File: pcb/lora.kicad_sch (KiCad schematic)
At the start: 57 parts, among them J1 Conn_01x04, J11 Conn_Coaxial, J2 5V, J3 Temp, J5 Temp, J6 VDD, J7 UART, J9 I2C, Q2 AO3401A, Q3 AO3401A, Q5 AO3401A, SW1 RESET, SW2 PJ, U1 ME2108C50M5G, U2 ESP32-WROOM-32D, U3 2460, U4 RFM95W-868S2

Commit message: schematic finalized
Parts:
- removed Q?: AO3400A, Package_TO_SOT_SMD:SOT-23, symbol Transistor_FET:AO3400A
- removed R?: 100, Resistor_SMD:R_0603_1608Metric, symbol Device:R_Small
- removed R?: 10k, Capacitor_SMD:C_0603_1608Metric, symbol Device:R_Small
- added C10: 2u2, Capacitor_SMD:C_0805_2012Metric, symbol Device:C_Small
- added C14, C16, C20: 100n, Capacitor_SMD:C_0603_1608Metric, symbol Device:C_Small
- added C15, C18, C8: 10u, Capacitor_SMD:C_0805_2012Metric, symbol Device:C_Small
- added C17: 100p, Capacitor_SMD:C_0603_1608Metric, symbol Device:C_Small
- added C19: 1u, Capacitor_SMD:C_0603_1608Metric, symbol Device:C_Small
- added C21, C4: 47u, Capacitor_SMD:C_1206_3216Metric, symbol Device:C_Small
- added D10, D4, D6, D7, D8, D9: D_TVS, Diode_SMD:D_0402_1005Metric, symbol Device:D_TVS
- added D3: D_MM1Z15, Diode_SMD:D_SOD-123, symbol Device:D_Zener
- added FB1: Ferrite, Inductor_SMD:L_0805_2012Metric, symbol Device:FerriteBead_Small
- added L3: 15u, OWN_PARTS:SLO0630H, symbol Device:L_Small
- added Q1: AO3401A, Package_TO_SOT_SMD:SOT-23, symbol Transistor_FET:AO3401A
- added R14, R18: 100k, Resistor_SMD:R_0603_1608Metric, symbol Device:R_Small
- added R21: 62k, Resistor_SMD:R_0603_1608Metric, symbol Device:R_Small
- added R22: 20k, Resistor_SMD:R_0603_1608Metric, symbol Device:R_Small
- added R23, R24: 1k, Capacitor_SMD:C_0603_1608Metric, symbol Device:R_Small
- added SW3: K3-1296S-E1, OWN_Parts_:K3-1296S-E1, symbol OWN_Parts_:K3-1296S-E1
- added U5: SCT2400, Package_TO_SOT_SMD:TSOT-23-6, symbol lv2842x:LV2842X
- J1: footprint (none) -> TerminalBlock_TE-Connectivity:TerminalBlock_TE_282834-4_1x04_P2.54mm_Horizontal
- J3: footprint Connector_PinHeader_2.54mm:PinHeader_1x03_P2.54mm_Horizontal -> TerminalBlock_TE-Connectivity:TerminalBlock_TE_282834-3_1x03_P2.54mm_Horizontal
- J6: footprint Connector_PinHeader_2.54mm:PinHeader_1x02_P2.54mm_Vertical -> TerminalBlock_TE-Connectivity:TerminalBlock_TE_282834-2_1x02_P2.54mm_Horizontal
- J7, J9: footprint Connector_PinHeader_2.54mm:PinHeader_1x04_P2.54mm_Vertical -> TerminalBlock_TE-Connectivity:TerminalBlock_TE_282834-4_1x04_P2.54mm_Horizontal
- U3: footprint SamacSys_Parts:2460 -> 2460
- gave numbers to parts that had none: 1
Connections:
- net EXT_ADC_SENSE: now also R24.1
- net EXT_ADC_SENSE2: now also R23.1
- net GND: now also D5.1 (A1), C10.2, C14.1, C15.2, C18.2, C19.2, C20.1, C21.1, C4.2, C8.2, D10.1 (A1), D4.1 (A1), D6.1 (A1), D7.1 (A1), D8.1 (A1), D9.1 (A1), R14.1, R22.2, SW3.4, U5.2 (GND)
- net I2C_SCL: now also D5.2 (A2)
- net I2C_SDA: now also D10.2 (A2)
- net ONEWIRE1_DATA: now also D4.2 (A2)
- net UART2_RX: now also D9.2 (A2)
- net UART2_TX: now also D8.2 (A2)
- net VDD: now also SW3.2; no longer J6.2 (Pin_2), Q5.2 (S)
- net at J1.2 (Pin_2): now also D7.2 (A2), R24.2
- net at J1.3 (Pin_3): now also D6.2 (A2), R23.2
- net +5V renamed BUCK_5V
- net GND_OFF: no longer names the net of U2.8 (IO32)
- new net: C10.1, C14.2, C4.1, C8.1, FB1.2, R18.2, U5.5 (VIN)
- new net: C17.2, R21.2, R22.1, U5.3 (FB)
- new net: D3.2 (A), Q1.1 (G), R14.2
- new net: R18.1, U5.4 (EN)
- new net: C16.1, L3.1, U5.6 (SW)
- new net: C16.2, U5.1 (CB)
- new net 3V3EXT: C17.1, C18.1, C19.1, C20.2, C21.2, L3.2, R21.1, SW3.3
- new net VBATT: Q5.2 (S), SW3.1
- new net VSUPPLY: C15.1, D3.1 (K), FB1.1, Q1.2 (S)
- new net VSUPPLY_IN: J6.2 (Pin_2), Q1.3 (D)
- no-connect marks 18 -> 19
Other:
- note added: "Battery stuff LS14500 (3.67V full at 20°C, 2.5V full at -20C and 100mA Discharge) Empty at 20C: < 3.2V at 55mA Discharge, < 3.4 at 10mA Discharge)"
- note added: "Not used GPIO"
- note added: "Program and Reset"
- note added: "Reverse polarity protection"
- note added: "Select Power Source"
- note added: "Terminal Connectors + ESD protection"
- note removed: "Auxilary connectors"
- note removed: "LS14500 (3.67V full at 20°C, 2.5V full at -20C and 100mA Discharge) Empty at 20C: < 3.2V at 55mA Discharge, < 3.4 at 10mA Discharge)"
- note removed: "One Wire Connector"
- note removed: "Pull to VDD => On Floating => Off"
- note removed: "esd protection!"
- note removed: "https://www.youtube.com/watch?v=LY-1DHTxRAk check for pin assignment!"
- moved on the sheet: C1, C13, C2, C5, D1, D5, H1, H3, J1, J2, J3, J5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

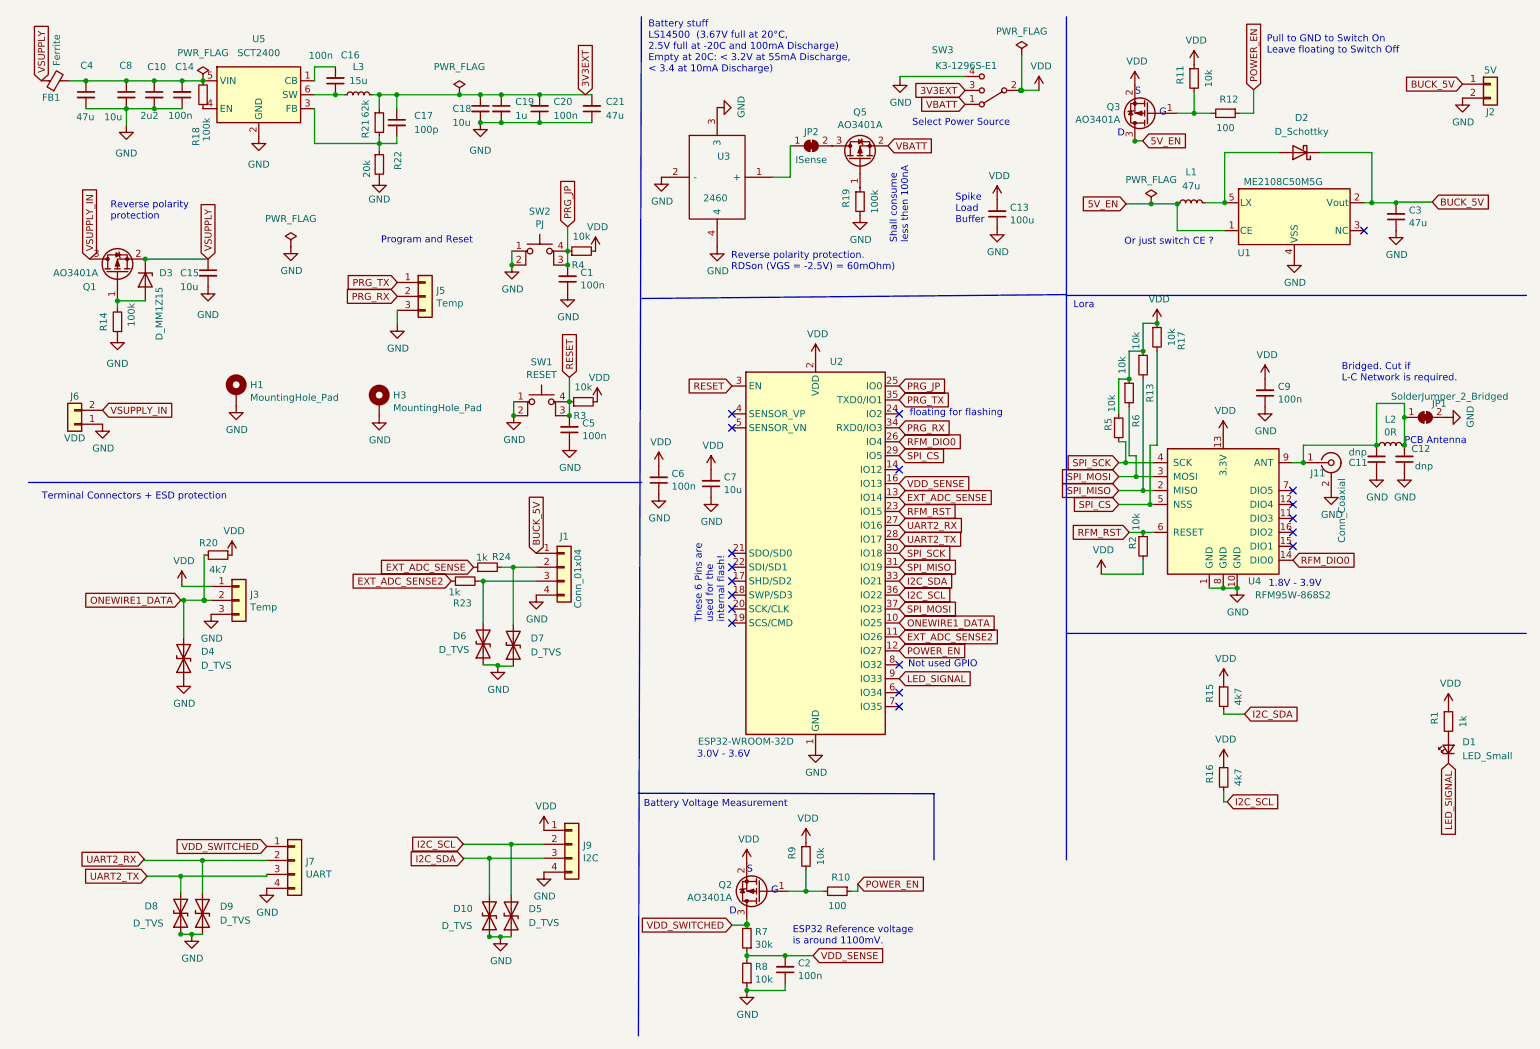
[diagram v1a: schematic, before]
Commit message: updated layout
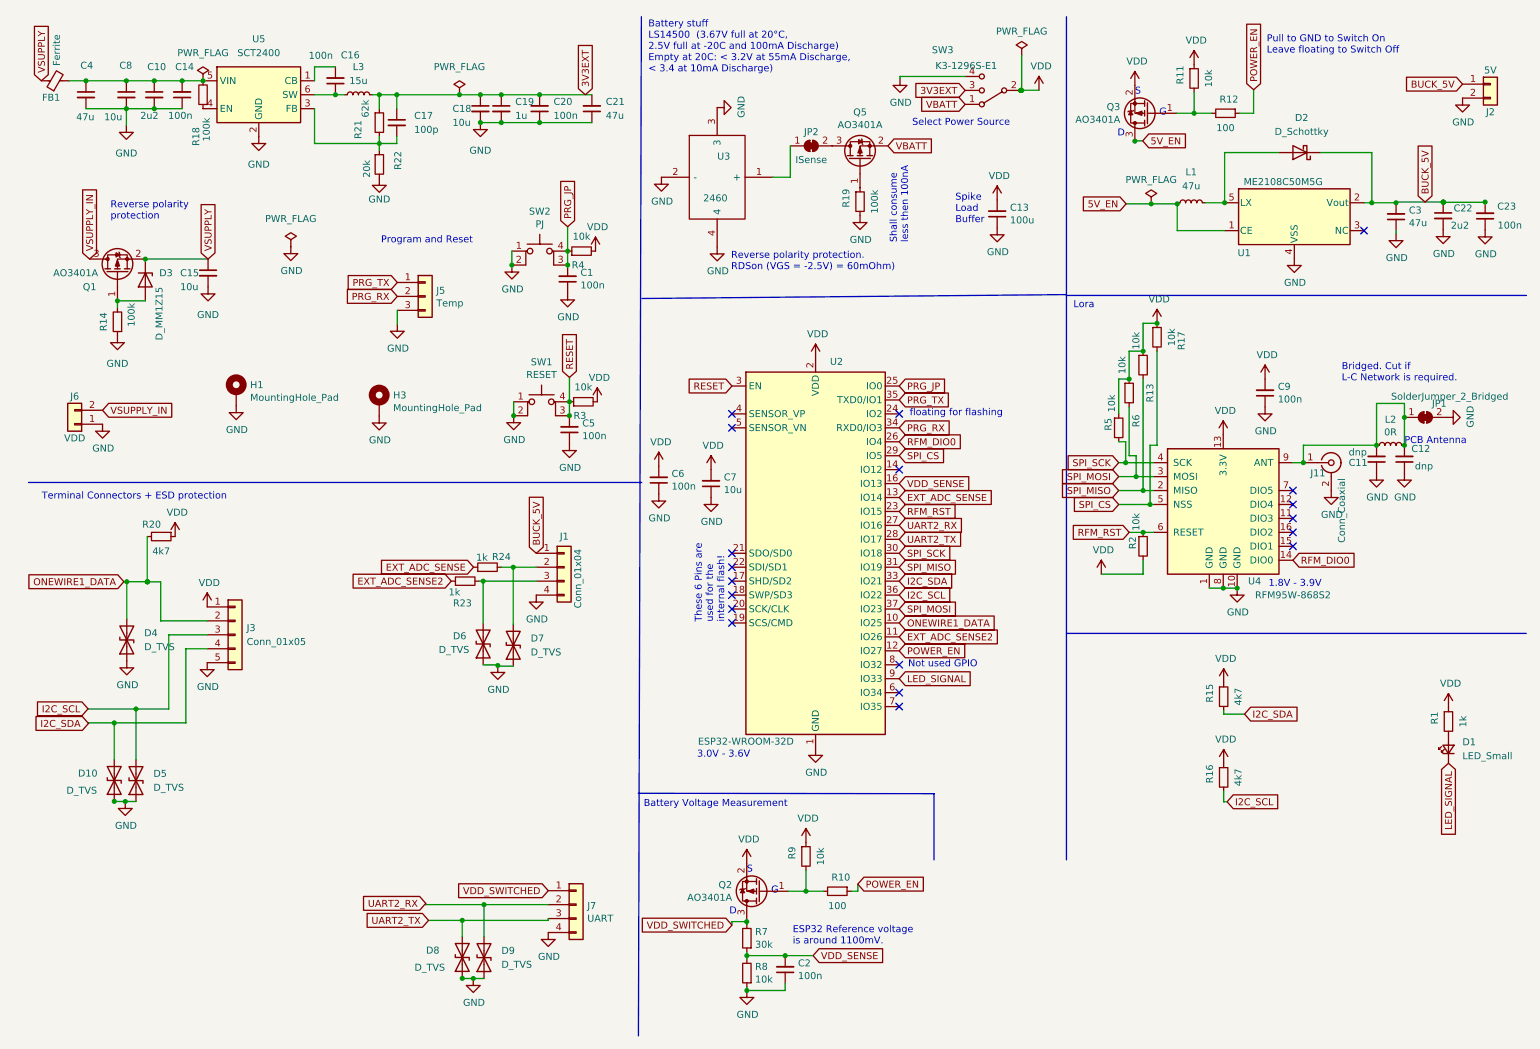
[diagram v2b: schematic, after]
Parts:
- removed J3: Temp, TerminalBlock_TE-Connectivity:TerminalBlock_TE_282834-3_1x03_P2.54mm_Horizontal, symbol Connector_Generic:Conn_01x03
- removed J9: I2C, TerminalBlock_TE-Connectivity:TerminalBlock_TE_282834-4_1x04_P2.54mm_Horizontal, symbol Connector_Generic:Conn_01x04
- added C22: 2u2, Capacitor_SMD:C_0805_2012Metric, symbol Device:C_Small
- added C23: 100n, Capacitor_SMD:C_0603_1608Metric, symbol Device:C_Small
- added J3: Conn_01x05, TerminalBlock_TE-Connectivity:TerminalBlock_TE_282834-5_1x05_P2.54mm_Horizontal, symbol Connector_Generic:Conn_01x05
- C3: footprint Capacitor_SMD:C_1206_3216Metric -> Capacitor_SMD:C_1210_3225Metric; LCSC (none) -> C77101
- C4: LCSC C96123 -> C403725
- D2: footprint (none) -> Diode_SMD:D_SOD-323
- J7: footprint TerminalBlock_TE-Connectivity:TerminalBlock_TE_282834-4_1x04_P2.54mm_Horizontal -> OWN_Parts_:pcb_edge_2_2
- U3: footprint 2460 -> SamacSys_Parts:2460
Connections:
- net BUCK_5V: now also C22.1, C23.2
- net GND: now also C22.2, C23.1, J3.5 (Pin_5)
- net I2C_SCL: now also J3.3 (Pin_3)
- net I2C_SDA: now also J3.4 (Pin_4)
- net ONEWIRE1_DATA: now also J3.2 (Pin_2)
- net VDD: now also J3.1 (Pin_1)
- net VDD_SWITCHED: now also Q2.3 (D), R7.2
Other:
- note removed: "Or just switch CE ?"
- moved on the sheet: D10, D4, D5, D8, D9, J7, R20

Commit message: updated layout
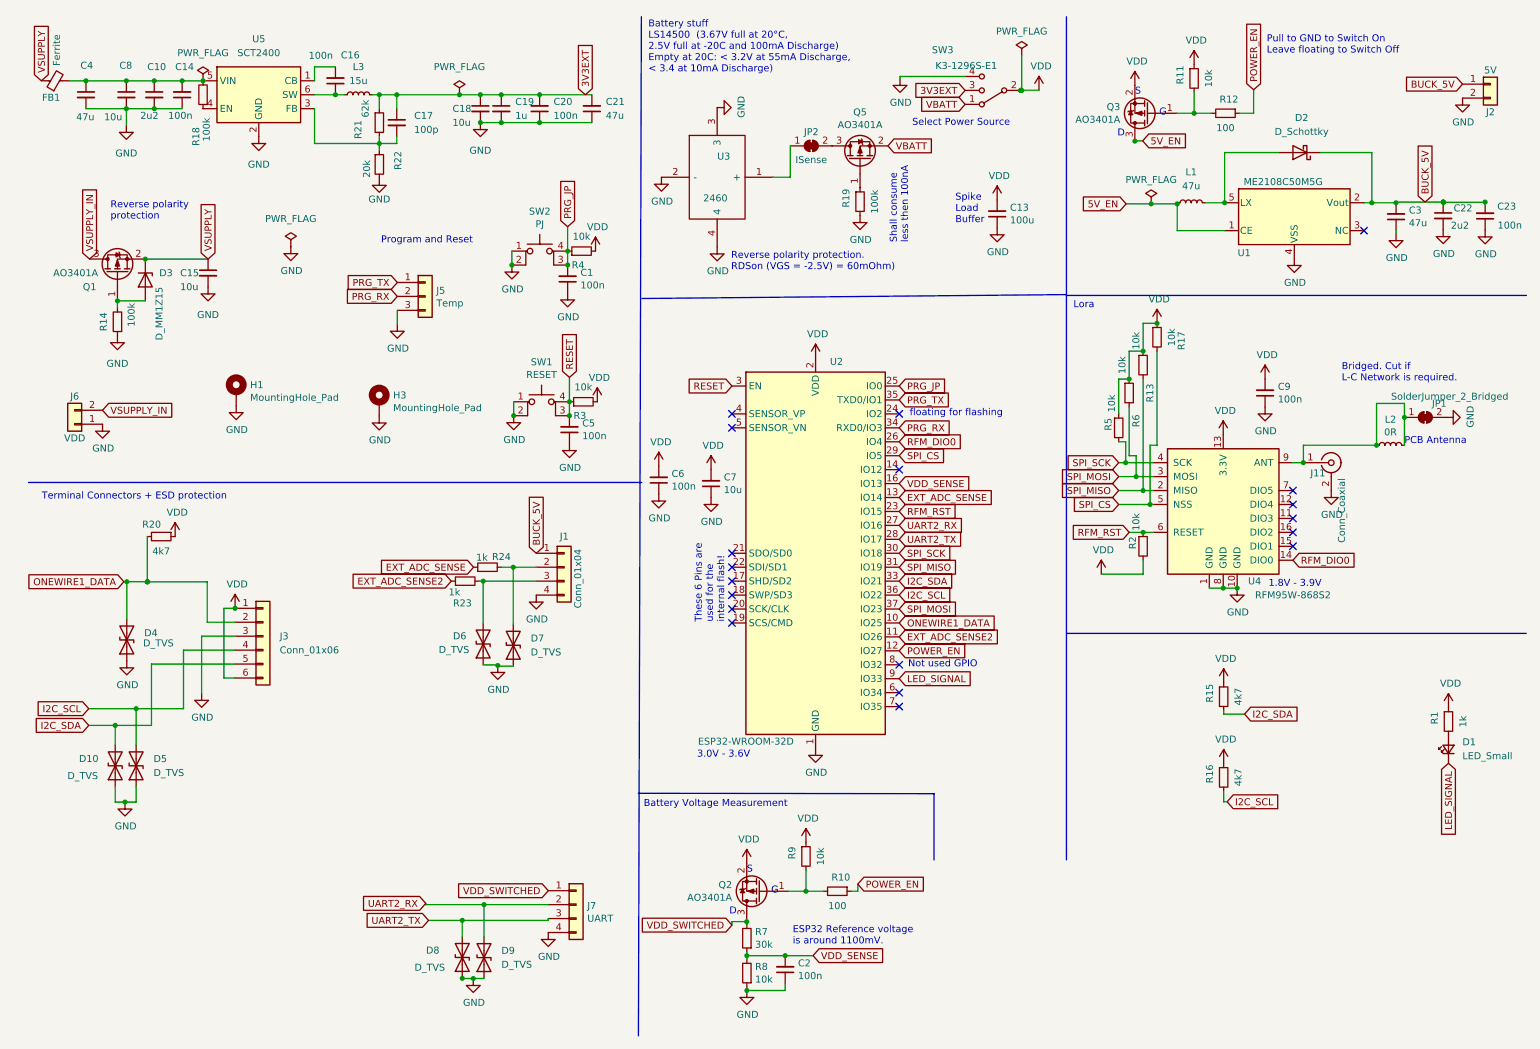
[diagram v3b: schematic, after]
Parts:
- removed C11, C12: dnp, Capacitor_SMD:C_0603_1608Metric, symbol Device:C_Small
- removed J3: Conn_01x05, TerminalBlock_TE-Connectivity:TerminalBlock_TE_282834-5_1x05_P2.54mm_Horizontal, symbol Connector_Generic:Conn_01x05
- added J3: Conn_01x06, TerminalBlock_TE-Connectivity:TerminalBlock_TE_282834-6_1x06_P2.54mm_Horizontal, symbol Connector_Generic:Conn_01x06
- JP1: footprint Jumper:SolderJumper-2_P1.3mm_Bridged_Pad1.0x1.5mm -> OWN_Parts_:jumperhidden
- JP2: footprint (none) -> Jumper:SolderJumper-2_P1.3mm_Bridged_RoundedPad1.0x1.5mm
- L3: footprint OWN_PARTS:SLO0630H -> OWN_Parts_:SLO0630H
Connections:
- net GND: now also J3.3 (Pin_3)
- net I2C_SCL: now also J3.4 (Pin_4)
- net I2C_SDA: now also J3.5 (Pin_5)
- net ONEWIRE1_DATA: now also J3.2 (Pin_2)
- net VDD: now also J3.1 (Pin_1), J3.6 (Pin_6)
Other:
- moved on the sheet: D10, D5

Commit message: added usb - serial and external power supply
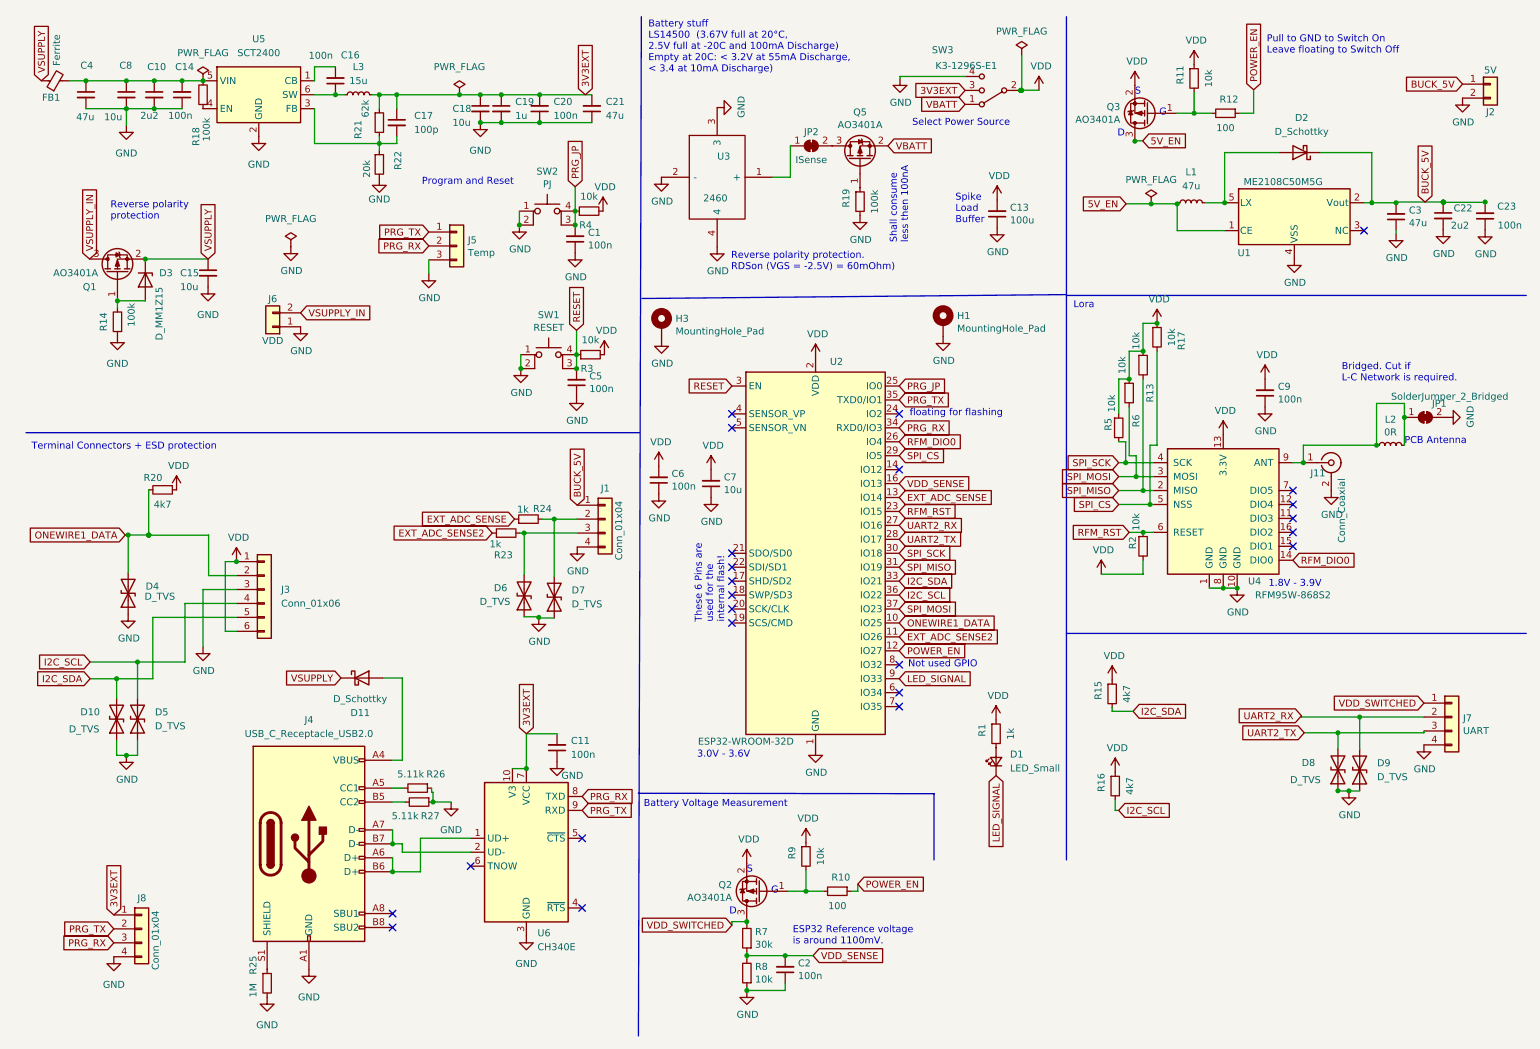
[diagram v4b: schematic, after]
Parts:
- added C11: 100n, Capacitor_SMD:C_0603_1608Metric, symbol Device:C_Small
- added D11: D_Schottky, Diode_SMD:D_SOD-323, symbol Device:D_Schottky
- added J4: USB_C_Receptacle_USB2.0, Connector_USB:USB_C_Receptacle_HRO_TYPE-C-31-M-12, symbol Connector:USB_C_Receptacle_USB2.0
- added J8: Conn_01x04, Connector_PinHeader_2.54mm:PinHeader_1x04_P2.54mm_Vertical, symbol Connector_Generic:Conn_01x04
- added R25: 1M, Resistor_SMD:R_0603_1608Metric, symbol Device:R_Small
- added R26, R27: 5.11k, Resistor_SMD:R_0603_1608Metric, symbol Device:R_Small
- added U6: CH340E, Package_SO:MSOP-10_3x3mm_P0.5mm, symbol Interface_USB:CH340E
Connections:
- net 3V3EXT: now also C11.2, J8.1 (Pin_1), U6.10 (V3), U6.7 (VCC)
- net GND: now also C11.1, J4.A1 (GND), J4.A12 (GND), J4.B1 (GND), J4.B12 (GND), J8.4 (Pin_4), R25.2, R26.1, R27.1, U6.3 (GND)
- net PRG_RX: now also J8.3 (Pin_3), U6.8 (TXD)
- net PRG_TX: now also J8.2 (Pin_2), U6.9 (RXD)
- net VSUPPLY: now also D11.1 (K)
- new net: J4.A5 (CC1), R26.2
- new net: D11.2 (A), J4.A4 (VBUS), J4.A9 (VBUS), J4.B4 (VBUS), J4.B9 (VBUS)
- new net: J4.A6 (D+), J4.B6 (D+), U6.1 (UD+)
- new net: J4.A7 (D-), J4.B7 (D-), U6.2 (UD-)
- new net: J4.B5 (CC2), R27.2
- new net: J4.S1 (SHIELD), R25.1
- no-connect marks 19 -> 24
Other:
- title: Lora Vision  -> AcreLink
- moved on the sheet: C1, C5, D1, D10, D4, D5, D6, D7, D8, D9, H1, H3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

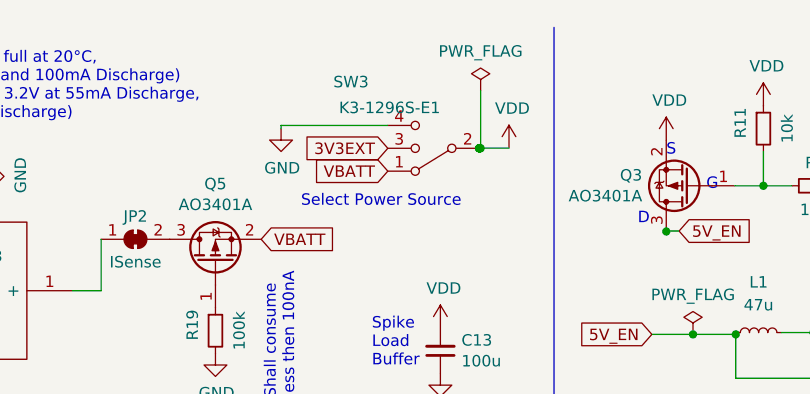
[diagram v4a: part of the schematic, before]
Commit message: fixed DRC errors
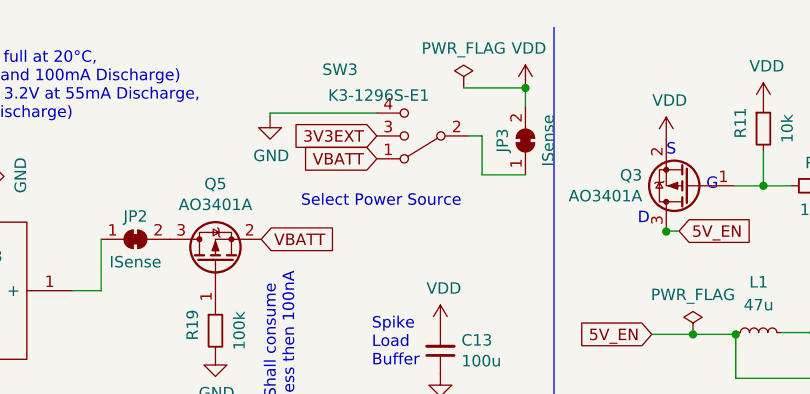
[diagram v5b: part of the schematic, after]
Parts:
- added JP3: ISense, Jumper:SolderJumper-2_P1.3mm_Bridged_RoundedPad1.0x1.5mm, symbol Jumper:SolderJumper_2_Bridged
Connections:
- net VDD: now also JP3.2 (B); no longer SW3.2
- new net: JP3.1 (A), SW3.2
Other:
- moved on the sheet: SW3
